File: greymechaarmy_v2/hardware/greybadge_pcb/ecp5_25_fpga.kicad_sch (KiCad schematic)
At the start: 18 parts, among them Q2 Q_NMOS_GSD, U8 ECP5U_25_CABGA256, U9 W25Q128JVSIM, X1 SiT2001B

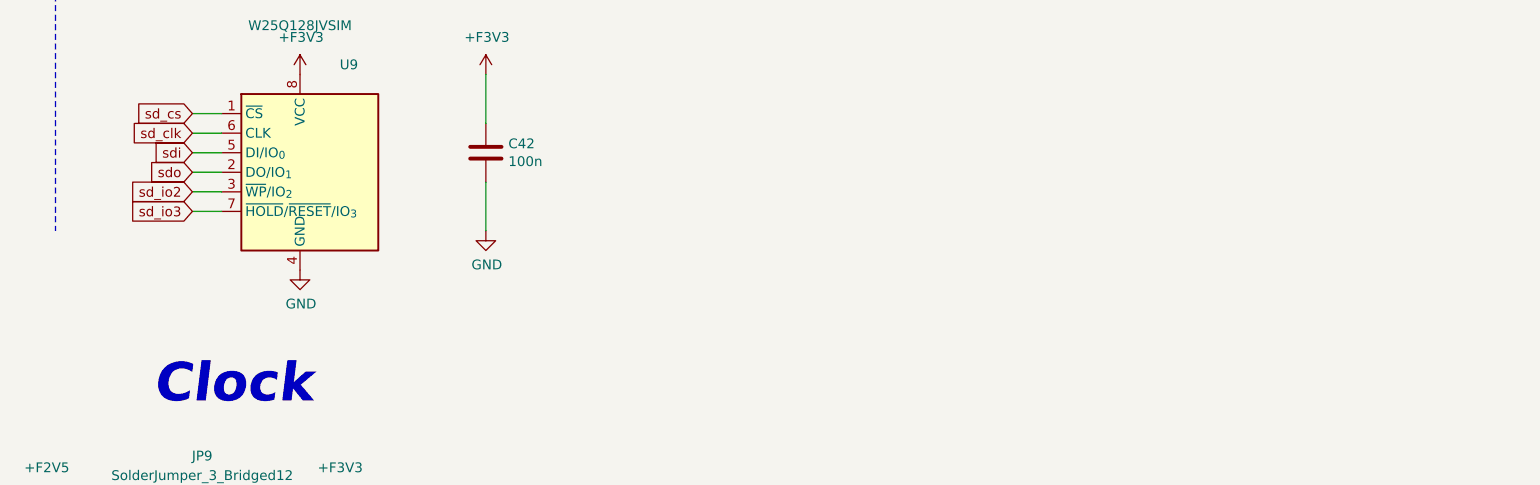
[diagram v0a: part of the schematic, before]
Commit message: fix: spi flash pinout
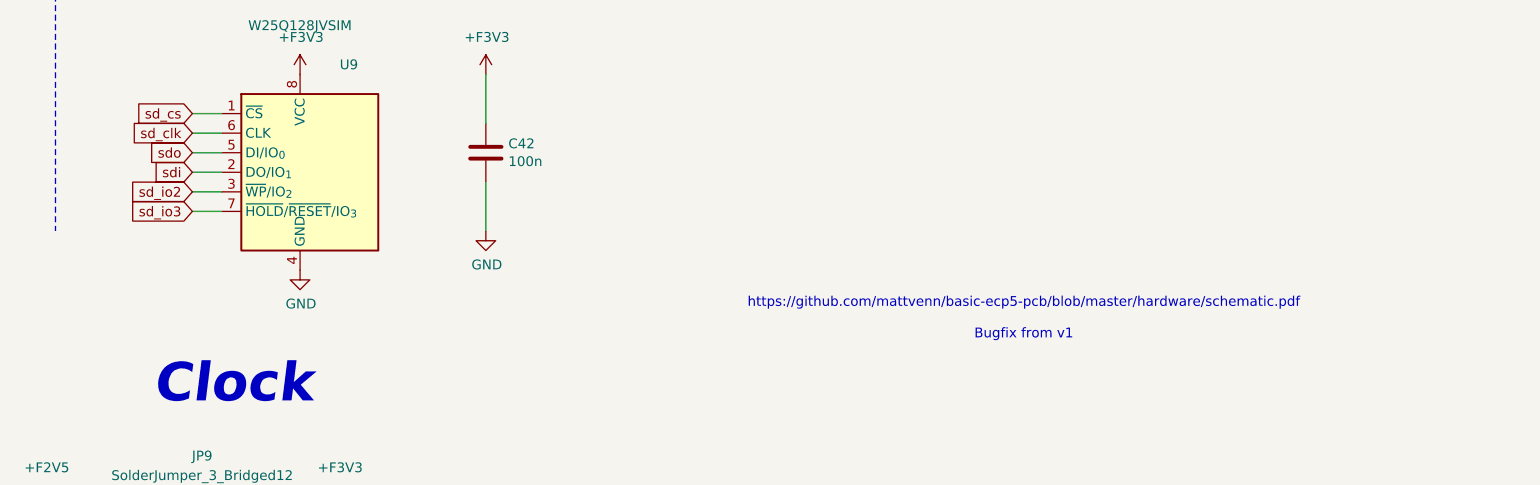
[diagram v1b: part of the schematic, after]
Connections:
- net sdi: now also U9.2 (DO/IO_{1}); no longer U9.5 (DI/IO_{0})
- net sdo: now also U9.5 (DI/IO_{0}); no longer U9.2 (DO/IO_{1})
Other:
- note added: "https://github.com/mattvenn/basic-ecp5-pcb/blob/master/hardware/schematic.pdf Bugfix from v1"

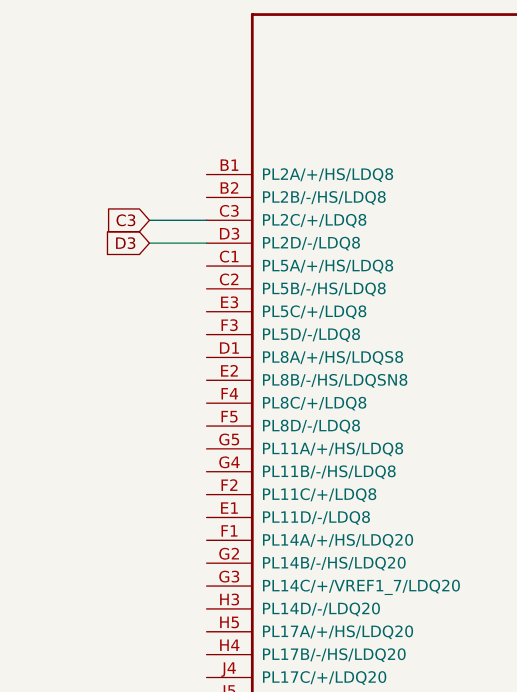
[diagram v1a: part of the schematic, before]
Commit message: feat: add additional pmod header with differential lines
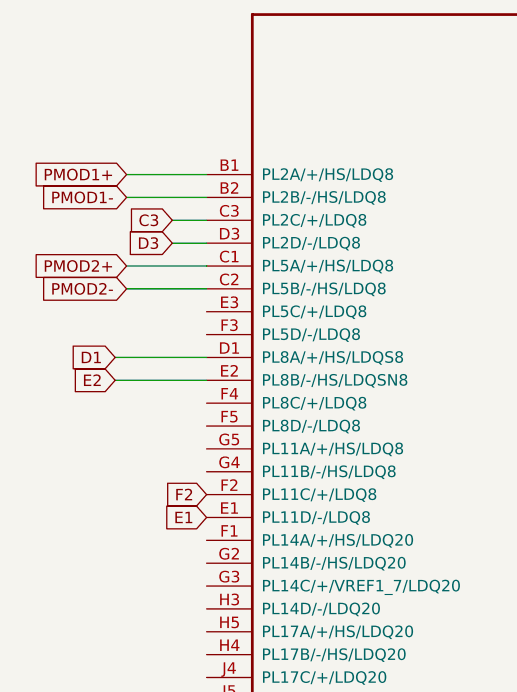
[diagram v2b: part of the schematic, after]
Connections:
- net PMOD1+: now reaches U8.B1 (PL2A/+/HS/LDQ8)
- net PMOD1-: now reaches U8.B2 (PL2B/-/HS/LDQ8)
- net PMOD2+: now reaches U8.C1 (PL5A/+/HS/LDQ8)
- net PMOD2-: now reaches U8.C2 (PL5B/-/HS/LDQ8)
- net D1: now reaches U8.D1 (PL8A/+/HS/LDQS8)
- net E1: now reaches U8.E1 (PL11D/-/LDQ8)
- net E2: now reaches U8.E2 (PL8B/-/HS/LDQSN8)
- net F2: now reaches U8.F2 (PL11C/+/LDQ8)
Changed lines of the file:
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@@
 	(wire
 		(pts
+			(xy 25.4 185.42) (xy 34.29 185.42)
+		)
+		(stroke
+			(width 0)
+			(type default)
+		)
+	)
+	(wire
+		(pts
 			(xy 29.21 57.15) (xy 36.83 57.15)
 		)
@@
 	(wire
 		(pts
+			(xy 24.13 208.28) (xy 34.29 208.28)
+		)
+		(stroke
+			(width 0)
+			(type default)
+		)
+	)
+	(wire
+		(pts
+			(xy 25.4 195.58) (xy 34.29 195.58)
+		)
+		(stroke
+			(width 0)
+			(type default)
+		)
+	)
+	(wire
+		(pts
 			(xy 149.86 278.13) (xy 149.86 273.05)
 		)
@@
 	(wire
 		(pts
-			(xy 27.94 190.5) (xy 34.29 190.5)
+			(xy 30.48 190.5) (xy 34.29 190.5)
 		)
 		(stroke
@@
 	(wire
 		(pts
+			(xy 24.13 205.74) (xy 34.29 205.74)
+		)
+		(stroke
+			(width 0)
+			(type default)
+		)
+	)
+	(wire
+		(pts
 			(xy 408.94 179.07) (xy 400.05 179.07)
 		)
@@
 	(wire
 		(pts
+			(xy 25.4 198.12) (xy 34.29 198.12)
+		)
+		(stroke
+			(width 0)
+			(type default)
+		)
+	)
+	(wire
+		(pts
 			(xy 138.43 278.13) (xy 134.62 278.13)
 		)
@@
 	(wire
 		(pts
-			(xy 27.94 193.04) (xy 34.29 193.04)
+			(xy 30.48 193.04) (xy 34.29 193.04)
 		)
 		(stroke
@@
 	(wire
 		(pts
+			(xy 25.4 187.96) (xy 34.29 187.96)
+		)
+		(stroke
+			(width 0)
+			(type default)
+		)
+	)
+	(wire
+		(pts
 			(xy 195.58 254) (xy 195.58 265.43)
 		)
@@
 		)
 	)
+	(global_label "E2"
+		(shape input)
+		(at 24.13 208.28 180)
+		(fields_autoplaced yes)
+		(effects
+			(font
+				(size 1.27 1.27)
+			)
+			(justify right)
+		)
+		(property "Intersheetrefs" "${INTERSHEET_REFS}"
+			(at 18.7863 208.28 0)
+			(effects
+				(font
+					(size 1.27 1.27)
+				)
+				(justify right)
+				(hide yes)
+			)
+		)
+	)
 	(global_label "sd_io2"
 		(shape input)
@@
 		)
 	)
+	(global_label "PMOD1-"
+		(shape input)
+		(at 25.4 187.96 180)
+		(fields_autoplaced yes)
+		(effects
+			(font
+				(size 1.27 1.27)
+			)
+			(justify right)
+		)
+		(property "Intersheetrefs" "${INTERSHEET_REFS}"
+			(at 14.311 187.96 0)
+			(effects
+				(font
+					(size 1.27 1.27)
+				)
+				(justify right)
+				(hide yes)
+			)
+		)
+	)
+	(global_label "F2"
+		(shape input)
+		(at 34.29 220.98 180)
+		(fields_autoplaced yes)
+		(effects
+			(font
+				(size 1.27 1.27)
+			)
+			(justify right)
+		)
+		(property "Intersheetrefs" "${INTERSHEET_REFS}"
+			(at 29.0067 220.98 0)
+			(effects
+				(font
+					(size 1.27 1.27)
+				)
+				(justify right)
+				(hide yes)
+			)
+		)
+	)
 	(global_label "B4"
 		(shape input)
@@
 		)
 	)
+	(global_label "E1"
+		(shape input)
+		(at 34.29 223.52 180)
+		(fields_autoplaced yes)
+		(effects
+			(font
+				(size 1.27 1.27)
+			)
+			(justify right)
+		)
+		(property "Intersheetrefs" "${INTERSHEET_REFS}"
+			(at 28.9463 223.52 0)
+			(effects
+				(font
+					(size 1.27 1.27)
+				)
+				(justify right)
+				(hide yes)
+			)
+		)
+	)
 	(global_label "sd_io3"
 		(shape input)
@@
 		)
 	)
+	(global_label "PMOD2+"
+		(shape input)
+		(at 25.4 195.58 180)
+		(fields_autoplaced yes)
+		(effects
+			(font
+				(size 1.27 1.27)
+			)
+			(justify right)
+		)
+		(property "Intersheetrefs" "${INTERSHEET_REFS}"
+			(at 14.311 195.58 0)
+			(effects
+				(font
+					(size 1.27 1.27)
+				)
+				(justify right)
+				(hide yes)
+			)
+		)
+	)
 	(global_label "D13"
 		(shape input)
@@
 		)
 	)
+	(global_label "PMOD1+"
+		(shape input)
+		(at 25.4 185.42 180)
+		(fields_autoplaced yes)
+		(effects
+			(font
+				(size 1.27 1.27)
+			)
+			(justify right)
+		)
+		(property "Intersheetrefs" "${INTERSHEET_REFS}"
+			(at 14.311 185.42 0)
+			(effects
+				(font
+					(size 1.27 1.27)
+				)
+				(justify right)
+				(hide yes)
+			)
+		)
+	)
 	(global_label "clk"
 		(shape input)
@@
 	(global_label "D3"
 		(shape input)
-		(at 27.94 193.04 180)
+		(at 30.48 193.04 180)
 		(fields_autoplaced yes)
 		(effects
@@
 		)
 		(property "Intersheetrefs" "${INTERSHEET_REFS}"
-			(at 22.4753 193.04 0)
+			(at 25.0153 193.04 0)
 			(effects
 				(font
@@
 	(global_label "C3"
 		(shape input)
-		(at 27.94 190.5 180)
+		(at 30.48 190.5 180)
 		(fields_autoplaced yes)
 		(effects
@@
 		)
 		(property "Intersheetrefs" "${INTERSHEET_REFS}"
-			(at 22.4753 190.5 0)
+			(at 25.0153 190.5 0)
 			(effects
 				(font
@@
 		)
 	)
+	(global_label "PMOD2-"
+		(shape input)
+		(at 25.4 198.12 180)
+		(fields_autoplaced yes)
+		(effects
+			(font
+				(size 1.27 1.27)
+			)
+			(justify right)
+		)
+		(property "Intersheetrefs" "${INTERSHEET_REFS}"
+			(at 14.311 198.12 0)
+			(effects
+				(font
+					(size 1.27 1.27)
+				)
+				(justify right)
+				(hide yes)
+			)
+		)
+	)
 	(global_label "B5"
 		(shape input)
@@
 				(hide yes)
 			)
+		)
+	)
+	(global_label "D1"
+		(shape input)
+		(at 24.13 205.74 180)
+		(fields_autoplaced yes)
+		(effects
+			(font
+				(size 1.27 1.27)
+			)
+			(justify right)
+		)
+		(property "Intersheetrefs" "${INTERSHEET_REFS}"
+			(at 18.6653 205.74 0)
+			(effects
+				(font
+					(size 1.27 1.27)
+				)
+				(justify right)
+				(hide yes)
+			)
